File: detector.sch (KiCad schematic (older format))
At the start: 40 parts, among them J1 Conn_01x01, J2 Conn_01x01, J3 Conn_01x01, J4 BATT, Q1 BF245A, Q2 BC847, SW1 1, SW2 2, SW3 3, SW4 4, U1 4049, U2 L78L05_SO8

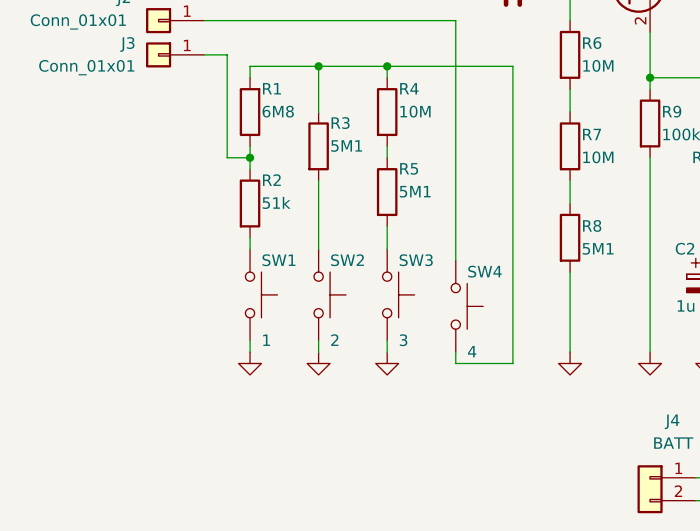
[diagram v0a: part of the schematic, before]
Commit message: Create all footprints
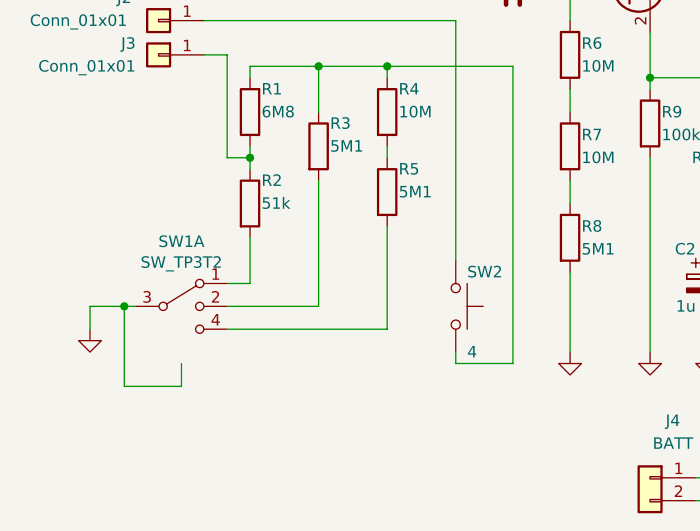
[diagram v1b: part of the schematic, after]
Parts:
- removed SW1: 1, Button_Switch_THT:SW_PUSH_6mm_H8mm, symbol Switch:SW_Push
- removed SW2: 2, Button_Switch_THT:SW_PUSH_6mm_H8mm, symbol Switch:SW_Push
- removed SW3: 3, Button_Switch_THT:SW_PUSH_6mm_H8mm, symbol Switch:SW_Push
- added SW1: SW_TP3T2, detector:SW_SP3T2, symbol detector:SW_TP3T2
- renumbered SW4 to SW2
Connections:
- net GND: now also SW1.10 (Shield), SW1.3, SW1.9 (Shield)
- net at R2.2: now also SW1.1
- net at R3.2: now also SW1.2
- net at R5.2: now also SW1.4
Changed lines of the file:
@@
 $EndComp
 $Comp
-L power:VCC #PWR016
+L power:VCC #PWR014
 U 1 1 5C0C0537
 P 10000 800
-F 0 "#PWR016" H 10000 650 50  0001 C CNN
+F 0 "#PWR014" H 10000 650 50  0001 C CNN
 F 1 "VCC" H 10050 1000 50  0000 C CNN
 F 2 "" H 10000 800 50  0001 C CNN
@@
 $EndComp
 $Comp
-L power:VCC #PWR014
+L power:VCC #PWR012
 U 1 1 5C0C0C45
 P 9700 800
-F 0 "#PWR014" H 9700 650 50  0001 C CNN
+F 0 "#PWR012" H 9700 650 50  0001 C CNN
 F 1 "VCC" H 9750 1000 50  0000 C CNN
 F 2 "" H 9700 800 50  0001 C CNN
@@
 $EndComp
 $Comp
-L power:GND #PWR017
+L power:GND #PWR015
 U 1 1 5C0C0FF4
 P 10900 1000
-F 0 "#PWR017" H 10900 750 50  0001 C CNN
+F 0 "#PWR015" H 10900 750 50  0001 C CNN
 F 1 "GND" H 10950 800 50  0001 C CNN
 F 2 "" H 10900 1000 50  0001 C CNN
@@
 $EndComp
 $Comp
-L power:GND #PWR015
+L power:GND #PWR013
 U 1 1 5C0C16C8
 P 9700 1950
-F 0 "#PWR015" H 9700 1700 50  0001 C CNN
+F 0 "#PWR013" H 9700 1700 50  0001 C CNN
 F 1 "GND" H 9750 1750 50  0001 C CNN
 F 2 "" H 9700 1950 50  0001 C CNN
@@
 	8200 4250 8200 4200
 $Comp
-L power:GND #PWR013
+L power:GND #PWR011
 U 1 1 5C0FA341
 P 8200 4850
-F 0 "#PWR013" H 8200 4600 50  0001 C CNN
+F 0 "#PWR011" H 8200 4600 50  0001 C CNN
 F 1 "GND" H 8250 4650 50  0001 C CNN
 F 2 "" H 8200 4850 50  0001 C CNN
@@
 	8200 4850 8200 4800
 $Comp
-L power:GND #PWR010
+L power:GND #PWR08
 U 1 1 5C107972
 P 7250 3650
-F 0 "#PWR010" H 7250 3400 50  0001 C CNN
+F 0 "#PWR08" H 7250 3400 50  0001 C CNN
 F 1 "GND" H 7300 3450 50  0001 C CNN
 F 2 "" H 7250 3650 50  0001 C CNN
@@
 Wire Wire Line
 	6650 3200 6750 3200
-$Comp
-L power:VCC #PWR012
-U 1 1 5C172E88
-P 8200 3100
-F 0 "#PWR012" H 8200 2950 50  0001 C CNN
-F 1 "VCC" H 8250 3300 50  0000 C CNN
-F 2 "" H 8200 3100 50  0001 C CNN
-F 3 "" H 8200 3100 50  0001 C CNN
-	1    8200 3100
-	1    0    0    -1
-$EndComp
-Wire Wire Line
-	8200 3100 8200 3200
 Wire Wire Line
 	3350 4050 3350 4000
@@
 	7700 3200 7550 3200
 $Comp
-L power:GND #PWR011
+L power:GND #PWR09
 U 1 1 5C19B167
 P 7700 3650
-F 0 "#PWR011" H 7700 3400 50  0001 C CNN
+F 0 "#PWR09" H 7700 3400 50  0001 C CNN
 F 1 "GND" H 7750 3450 50  0001 C CNN
 F 2 "" H 7700 3650 50  0001 C CNN
@@
 Wire Wire Line
 	6750 3300 6750 3200
-Connection ~ 6750 3200
-Wire Wire Line
-	6750 3200 6950 3200
-$Comp
-L power:GND #PWR09
+$Comp
+L power:GND #PWR07
 U 1 1 5C1B7CCD
 P 6750 3650
-F 0 "#PWR09" H 6750 3400 50  0001 C CNN
+F 0 "#PWR07" H 6750 3400 50  0001 C CNN
 F 1 "GND" H 6800 3450 50  0001 C CNN
 F 2 "" H 6750 3650 50  0001 C CNN
@@
 	3600 4600 3600 4400
 $Comp
-L power:GND #PWR06
+L power:GND #PWR04
 U 1 1 5C1D3C87
 P 3600 5200
-F 0 "#PWR06" H 3600 4950 50  0001 C CNN
+F 0 "#PWR04" H 3600 4950 50  0001 C CNN
 F 1 "GND" H 3650 5000 50  0001 C CNN
 F 2 "" H 3600 5200 50  0001 C CNN
@@
 	3350 4000 3350 3800
 $Comp
-L power:GND #PWR05
+L power:GND #PWR03
 U 1 1 5C1F9B18
 P 3350 5200
-F 0 "#PWR05" H 3350 4950 50  0001 C CNN
+F 0 "#PWR03" H 3350 4950 50  0001 C CNN
 F 1 "GND" H 3400 5000 50  0001 C CNN
 F 2 "" H 3350 5200 50  0001 C CNN
@@
 $EndComp
 $Comp
-L power:GND #PWR04
+L power:GND #PWR02
 U 1 1 5C1FA466
 P 3000 5200
-F 0 "#PWR04" H 3000 4950 50  0001 C CNN
+F 0 "#PWR02" H 3000 4950 50  0001 C CNN
 F 1 "GND" H 3050 5000 50  0001 C CNN
 F 2 "" H 3000 5200 50  0001 C CNN
@@
 	7700 2850 7700 3200
 $Comp
-L Switch:SW_Push SW1
-U 1 1 5C2082AA
-P 1600 4950
-F 0 "SW1" V 1450 5000 50  0000 L CNN
-F 1 "1" V 1800 5000 50  0000 L CNN
-F 2 "Button_Switch_THT:SW_PUSH_6mm_H8mm" H 1600 5150 50  0001 C CNN
-F 3 "" H 1600 5150 50  0001 C CNN
-	1    1600 4950
-	0    1    1    0
-$EndComp
-$Comp
-L Switch:SW_Push SW2
-U 1 1 5C209FA5
-P 1900 4950
-F 0 "SW2" V 1750 5000 50  0000 L CNN
-F 1 "2" V 2100 5000 50  0000 L CNN
-F 2 "Button_Switch_THT:SW_PUSH_6mm_H8mm" H 1900 5150 50  0001 C CNN
-F 3 "" H 1900 5150 50  0001 C CNN
-	1    1900 4950
-	0    1    1    0
-$EndComp
-$Comp
-L Switch:SW_Push SW3
-U 1 1 5C20A285
-P 2200 4950
-F 0 "SW3" V 2050 5000 50  0000 L CNN
-F 1 "3" V 2400 5000 50  0000 L CNN
-F 2 "Button_Switch_THT:SW_PUSH_6mm_H8mm" H 2200 5150 50  0001 C CNN
-F 3 "" H 2200 5150 50  0001 C CNN
-	1    2200 4950
-	0    1    1    0
-$EndComp
-$Comp
-L power:GND #PWR03
-U 1 1 5C20A99E
-P 2200 5200
-F 0 "#PWR03" H 2200 4950 50  0001 C CNN
-F 1 "GND" H 2250 5000 50  0001 C CNN
-F 2 "" H 2200 5200 50  0001 C CNN
-F 3 "" H 2200 5200 50  0001 C CNN
-	1    2200 5200
-	1    0    0    -1
-$EndComp
-Wire Wire Line
-	2200 5200 2200 5150
-$Comp
-L power:GND #PWR02
-U 1 1 5C20C9DD
-P 1900 5200
-F 0 "#PWR02" H 1900 4950 50  0001 C CNN
-F 1 "GND" H 1950 5000 50  0001 C CNN
-F 2 "" H 1900 5200 50  0001 C CNN
-F 3 "" H 1900 5200 50  0001 C CNN
-	1    1900 5200
-	1    0    0    -1
-$EndComp
-Wire Wire Line
-	1900 5200 1900 5150
-$Comp
-L power:GND #PWR01
-U 1 1 5C20E976
-P 1600 5200
-F 0 "#PWR01" H 1600 4950 50  0001 C CNN
-F 1 "GND" H 1650 5000 50  0001 C CNN
-F 2 "" H 1600 5200 50  0001 C CNN
-F 3 "" H 1600 5200 50  0001 C CNN
-	1    1600 5200
-	1    0    0    -1
-$EndComp
-Wire Wire Line
-	1600 4750 1600 4700
-Wire Wire Line
-	1900 4750 1900 4450
-$Comp
-L power:GND #PWR08
+L power:GND #PWR05
 U 1 1 5C21EFF1
 P 3650 5850
-F 0 "#PWR08" H 3650 5600 50  0001 C CNN
+F 0 "#PWR05" H 3650 5600 50  0001 C CNN
 F 1 "GND" H 3700 5650 50  0001 C CNN
 F 2 "" H 3650 5850 50  0001 C CNN
@@
 	4150 4950 4200 4950
 $Comp
-L power:GND #PWR07
+L power:GND #PWR06
 U 1 1 5C2440EA
 P 4000 5200
-F 0 "#PWR07" H 4000 4950 50  0001 C CNN
+F 0 "#PWR06" H 4000 4950 50  0001 C CNN
 F 1 "GND" H 4050 5000 50  0001 C CNN
 F 2 "" H 4000 5200 50  0001 C CNN
@@
 $EndComp
 $Comp
-L Switch:SW_Push SW4
+L Switch:SW_Push SW2
 U 1 1 5C29A026
 P 2500 5000
-F 0 "SW4" V 2350 5050 50  0000 L CNN
+F 0 "SW2" V 2350 5050 50  0000 L CNN
 F 1 "4" V 2700 5050 50  0000 L CNN
 F 2 "Button_Switch_THT:SW_PUSH_6mm_H8mm" H 2500 5200 50  0001 C CNN
@@
 Wire Wire Line
 	1600 4300 1600 4350
-Wire Wire Line
-	1600 5200 1600 5150
 Wire Wire Line
 	1400 3900 1500 3900
@@
 Wire Wire Line
 	2200 4300 2200 4350
-Wire Wire Line
-	2200 4650 2200 4750
 $Comp
 L Device:R R10
@@
 	1    0    0    -1
 $EndComp
+Wire Wire Line
+	1500 4900 1600 4900
+Wire Wire Line
+	1600 4700 1600 4900
+Wire Wire Line
+	1500 5000 1900 5000
+Wire Wire Line
+	1900 4450 1900 5000
+Wire Wire Line
+	1500 5100 2200 5100
+Wire Wire Line
+	2200 4650 2200 5100
+$Comp
+L power:GND #PWR01
+U 1 1 5C5267AD
+P 900 5100
+F 0 "#PWR01" H 900 4850 50  0001 C CNN
+F 1 "GND" H 950 4900 50  0001 C CNN
+F 2 "" H 900 5100 50  0001 C CNN
+F 3 "" H 900 5100 50  0001 C CNN
+	1    900  5100
+	1    0    0    -1
+$EndComp
+Wire Wire Line
+	900  5100 900  5000
+Wire Wire Line
+	900  5000 1050 5000
+Wire Wire Line
+	1050 5350 1050 5000
+Connection ~ 1050 5000
+Wire Wire Line
+	1050 5000 1100 5000
+Wire Wire Line
+	1300 5250 1300 5350
+Wire Wire Line
+	6750 3200 6950 3200
+Connection ~ 6750 3200
+Wire Wire Line
+	1050 5350 1300 5350
+$Comp
+L power:VCC #PWR010
+U 1 1 5C172E88
+P 8200 3100
+F 0 "#PWR010" H 8200 2950 50  0001 C CNN
+F 1 "VCC" H 8250 3300 50  0000 C CNN
+F 2 "" H 8200 3100 50  0001 C CNN
+F 3 "" H 8200 3100 50  0001 C CNN
+	1    8200 3100
+	1    0    0    -1
+$EndComp
+Wire Wire Line
+	8200 3100 8200 3200
+$Comp
+L detector:SW_TP3T2 SW1
+U 1 1 5C581FE8
+P 1300 5000
+F 0 "SW1" H 1300 5283 50  0000 C CNN
+F 1 "SW_TP3T2" H 1300 5192 50  0000 C CNN
+F 2 "detector:SW_SP3T2" H 1000 5100 50  0001 C CNN
+F 3 "~" H 675 5175 50  0001 C CNN
+	1    1300 5000
+	1    0    0    -1
+$EndComp
